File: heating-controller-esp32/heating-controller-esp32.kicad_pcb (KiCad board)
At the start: 2 copper layers, 96.6 x 146.8 mm, 110 parts, among them J1 431151015826, J10 76829-0104, J11 USB_C_Receptacle_USB2.0, J2 431151015826, J3 76829-0104, J4 76829-0104, J5 76829-0104, J6 76829-0104, J7 76829-0104, J8 76829-0104, J9 76829-0104, Q1 MBT3904DW1, U1 ESP32-WROOM-32U, U10 MOC3061M, U2 CP2102N-A01-GQFN28, U4 MOC3061M, U6 MOC3061M, U7 MOC3061M, U8 MOC3061M, U9 MOC3061M

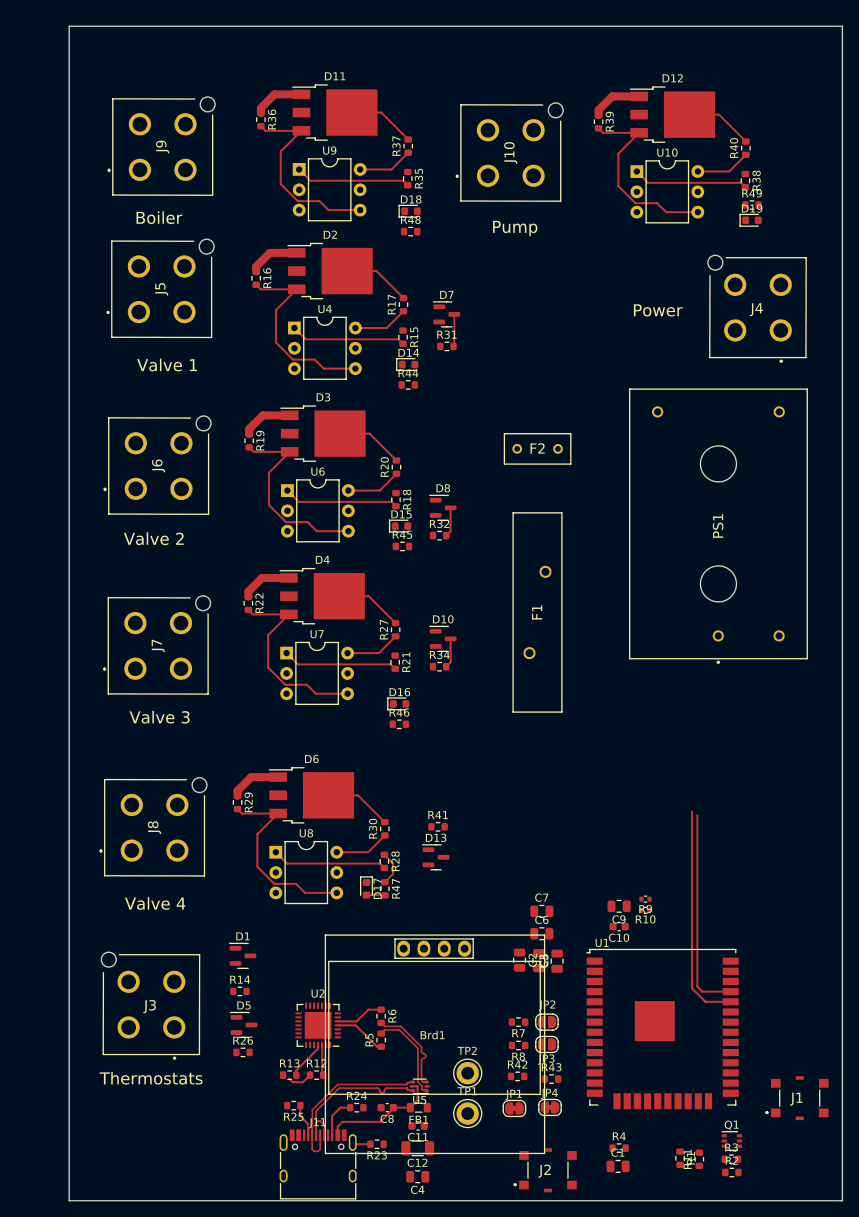
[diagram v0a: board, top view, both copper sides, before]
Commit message: Changed to Wago connectors; initial routing completed
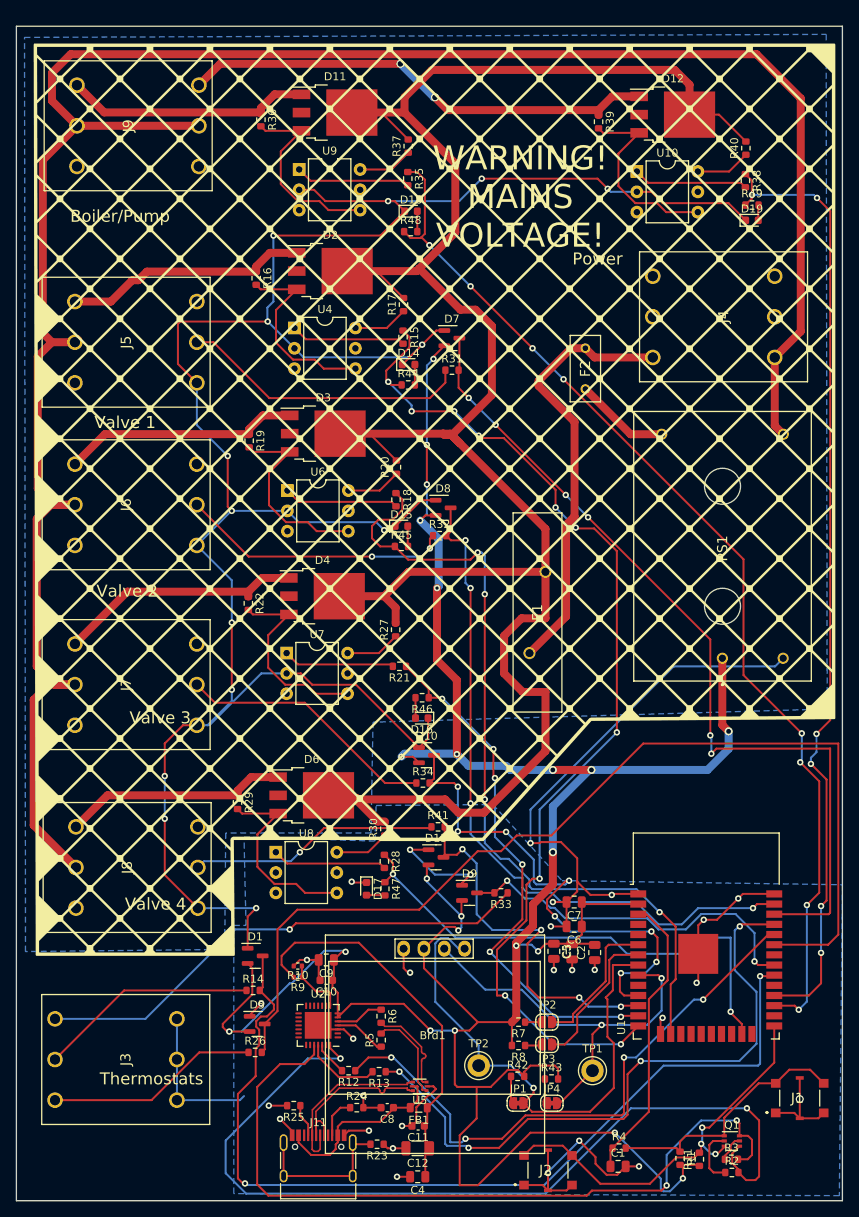
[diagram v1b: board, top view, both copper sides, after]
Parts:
- removed J10: 76829-0104, SamacSys_Parts:768290104
- added D9: ~, Package_TO_SOT_SMD:SOT-23, F.Cu at (66.5, 136.5)
- added R33: ~, Resistor_SMD:R_0603_1608Metric, F.Cu at (70.5, 136.5)
- J3, J4, J5, J6, J7, J8, J9: footprint SamacSys_Parts:768290104 -> SamacSys_Parts:736303
- U1: footprint RF_Module:ESP32-WROOM-32U -> RF_Module:ESP32-WROOM-32
- moved R9 44.5 mm to (45.1, 147.1)
- moved R10 44.0 mm to (45.1, 145.7)
- moved C9 37.2 mm to (48.6, 144.9)
- moved C10 37.2 mm to (48.6, 147.4)
- moved TP1 16.5 mm to (81.9, 158.8)
- moved R34 14.7 mm to (60.7, 122.8)
- moved D10 14.7 mm to (61.2, 119.3)
- moved J9 13.0 mm to (17.5, 35.6)
- moved J3 12.3 mm to (30.0, 162.4), turned to 90 degrees
- moved F2 11.7 mm to (81.0, 71.0), turned to -90 degrees
- moved R13 11.2 mm to (55.2, 158.9), turned to 180 degrees
- moved J5 10.8 mm to (17.2, 62.6)
- moved J6 10.3 mm to (17.2, 82.9)
- moved J7 10.3 mm to (17.2, 105.4)
- moved U1 10.0 mm to (96.1, 144.9)
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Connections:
- C10 pad 1: /ESP32/ESP_VDD -> +3V3
- C2 pad 2: /ESP32/ESP_VDD -> +3V3
- C3 pad 1: /ESP32/ESP_VDD -> +3V3
- C5 pad 2: /ESP32/ESP_VDD -> +3V3
- C6 pad 1: /ESP32/ESP_VDD -> +3V3
- C7 pad 1: /ESP32/ESP_VDD -> +3V3
- C9 pad 1: /ESP32/ESP_VDD -> +3V3
- D11 pad 1: /Boiler Out/Neutral -> /Boiler Out/Switched
- D12 pad 1: /Pump Out/Neutral -> /Pump Out/Switched
- D2 pad 1: /Valve Out 1/Neutral -> /Valve Out 1/Switched
- D3 pad 1: /Valve Out 2/Neutral -> /Valve Out 2/Switched
- D4 pad 1: /Valve Out 3/Neutral -> /Valve Out 3/Switched
- D6 pad 1: /Valve Out 4/Neutral -> /Valve Out 4/Switched
- J3 pad 1: /DHW_Thermostat -> GND
- J3 pad 2: GND -> /DHW_Thermostat
- J3 pad 3: /Spare_Thermostat -> GND
- J3 pad 4: GND -> /Spare_Thermostat
- J4 pad 1: unconnected-(J4-Pad1) -> NEUT
- J4 pad 2: Earth -> Net-(F1-Pad1)
- J4 pad 3: Net-(F1-Pad1) -> Earth
- J4 pad 4: NEUT -> unconnected-(J4-Pad4)
- J5 pad 1: /Valve_Microswitch_1 -> /Valve Out 1/Switched
- J5 pad 2: GND -> unconnected-(J5-Pad2)
- J5 pad 4: /Valve Out 1/Neutral -> /Valve_Microswitch_1
- J6 pad 1: /Valve_Microswitch_2 -> /Valve Out 2/Switched
- J6 pad 2: GND -> unconnected-(J6-Pad2)
- J6 pad 4: /Valve Out 2/Neutral -> /Valve_Microswitch_2
- J7 pad 1: /Valve_Microswitch_3 -> /Valve Out 3/Switched
- J7 pad 2: GND -> unconnected-(J7-Pad2)
- J7 pad 4: /Valve Out 3/Neutral -> /Valve_Microswitch_3
- J8 pad 1: /Valve_Microswitch_4 -> /Valve Out 4/Switched
- J8 pad 2: GND -> unconnected-(J8-Pad2)
- J8 pad 4: /Valve Out 4/Neutral -> /Valve_Microswitch_4
- J9 pad 1: Earth -> /Boiler Out/Switched
- J9 pad 2: unconnected-(J9-Pad2) -> /Pump Out/Switched
- J9 pad 4: /Boiler Out/Neutral -> NEUT
- R1 pad 1: /ESP32/ESP_VDD -> +3V3
- R11 pad 1: /ESP32/ESP_VDD -> +3V3
- R16 pad 1: /Valve Out 1/Neutral -> /Valve Out 1/Switched
- R19 pad 1: /Valve Out 2/Neutral -> /Valve Out 2/Switched
- R22 pad 1: /Valve Out 3/Neutral -> /Valve Out 3/Switched
- R29 pad 1: /Valve Out 4/Neutral -> /Valve Out 4/Switched
- R36 pad 1: /Boiler Out/Neutral -> /Boiler Out/Switched
- R39 pad 1: /Pump Out/Neutral -> /Pump Out/Switched
- R42 pad 2: 3.3V -> +3V3
- R43 pad 2: 3.3V -> +3V3
- U1 pad 2: /ESP32/ESP_VDD -> +3V3
- U2 pad 6: /ESP32/ESP_VDD -> +3V3
- U2 pad 7: /ESP32/ESP_VDD -> +3V3
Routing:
- net GND: track 0.00 -> 506.7 mm, vias 0 -> 43
- net +3V3: track 0.00 -> 347.5 mm, vias 0 -> 22
- net NEUT: track 0.00 -> 279.2 mm
- net LINE: track 50.6 -> 289.7 mm
- net /Boiler Out/Trigger: track 0.00 -> 134.1 mm, vias 0 -> 8
- net /ESP32/IO12: track 0.00 -> 132.4 mm, vias 0 -> 10
- net /ESP32/IO21: track 0.00 -> 128.3 mm
- net /ESP32/IO17: track 0.00 -> 120.3 mm, vias 0 -> 6
- net /ESP32/IO18: track 0.00 -> 116.1 mm, vias 0 -> 2
- net /ESP32/DTR: track 0.00 -> 111.8 mm, vias 0 -> 2
- net /ESP32/IO22: track 4.04 -> 107.8 mm, vias 0 -> 6
- net /ESP32/IO13: track 0.00 -> 102.6 mm, vias 0 -> 4
- net /ESP32/RTS: track 0.00 -> 96.5 mm, vias 0 -> 2
- net /ESP32/IO23: track 3.73 -> 87.8 mm, vias 0 -> 4
- net /ESP32/IO14: track 0.00 -> 66.3 mm, vias 0 -> 6
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- added copper zone on B.Cu, net Earth
- added copper zone on B.Cu, net GND
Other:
- board size 96.6 x 146.8 mm -> 103.3 x 146.8 mm
- board text added: "Boiler/Pump"
- board text added: "WARNING! MAINS VOLTAGE!"
- board text removed: "Boiler"
- board text removed: "Pump"

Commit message: Minor tweaks
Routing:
- net +3V3: track 347.5 -> 342.3 mm
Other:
- board text added: "Boot"
- board text added: "Reset"
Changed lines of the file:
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@@
+    (effects (font (size 1.5 1.5) (thickness 0.3)))
+  )
+  (gr_text "Reset" (at 107.95 167.386) (layer "F.SilkS")
     (effects (font (size 1.5 1.5) (thickness 0.3)))
   )
@@
     (effects (font (size 1.5 1.5) (thickness 0.3)))
   )
-  (gr_text "Power" (at 82.55 57.277) (layer "F.SilkS")
+  (gr_text "Power" (at 82.677 62.484) (layer "F.SilkS")
     (effects (font (size 1.5 1.5) (thickness 0.3)))
   )
   (gr_text "Boiler/Pump" (at 22.86 51.943) (layer "F.SilkS")
+    (effects (font (size 1.5 1.5) (thickness 0.3)))
+  )
+  (gr_text "Boot" (at 67.056 170.942) (layer "F.SilkS")
     (effects (font (size 1.5 1.5) (thickness 0.3)))
   )
@@
   (segment (start 72.39 142.748) (end 72.39 143.129) (width 1) (layer "F.Cu") (net 5))
   (segment (start 64.9605 109.9185) (end 62.484 107.442) (width 1) (layer "F.Cu") (net 5))
-  (segment (start 67.437 164.719) (end 65.315489 166.840511) (width 0.25) (layer "F.Cu") (net 5))
   (segment (start 76.068 142.88) (end 75.1205 143.8275) (width 0.25) (layer "F.Cu") (net 5))
   (segment (start 77.089 142.88) (end 82.042 142.88) (width 0.25) (layer "F.Cu") (net 5))
   (segment (start 71.84552 155.60152) (end 71.84552 152.68052) (width 0.25) (layer "F.Cu") (net 5))
   (segment (start 61.026 89.342) (end 60.3885 89.9795) (width 0.25) (layer "F.Cu") (net 5))
+  (segment (start 65.315489 166.840511) (end 67.437 164.719) (width 0.25) (layer "F.Cu") (net 5))
+  (segment (start 65.315489 169.380511) (end 65.315489 166.840511) (width 0.25) (layer "F.Cu") (net 5))
   (segment (start 98.151 115.55) (end 98.933 116.332) (width 1) (layer "F.Cu") (net 5))
   (segment (start 73.38352 159.46252) (end 73.38352 158.89948) (width 0.25) (layer "F.Cu") (net 5))
@@
   (segment (start 77.089 142.88) (end 76.068 142.88) (width 0.25) (layer "F.Cu") (net 5))
   (segment (start 60.85 145.94) (end 60.85 143.498) (width 0.25) (layer "F.Cu") (net 5))
-  (segment (start 74.168 166.497) (end 84.709 166.497) (width 0.25) (layer "F.Cu") (net 5))
   (segment (start 50.607 143.891) (end 49.591 144.907) (width 0.25) (layer "F.Cu") (net 5))
   (segment (start 35.697783 152.908) (end 35.697783 153.299783) (width 0.25) (layer "F.Cu") (net 5))
@@
   (segment (start 38.8135 145.349) (end 39.39652 145.93202) (width 0.25) (layer "F.Cu") (net 5))
   (segment (start 51.054 143.891) (end 50.607 143.891) (width 0.25) (layer "F.Cu") (net 5))
-  (segment (start 67.437 160.782) (end 67.437 164.719) (width 0.25) (layer "F.Cu") (net 5))
   (segment (start 80.579 137.668) (end 80.833 137.922) (width 0.25) (layer "F.Cu") (net 5))
   (segment (start 92.86352 170.52352) (end 95.14952 170.52352) (width 0.25) (layer "F.Cu") (net 5))
@@
   (segment (start 67.59052 152.68052) (end 60.85 145.94) (width 0.25) (layer "F.Cu") (net 5))
   (segment (start 74.168 158.115) (end 77.216 158.115) (width 0.25) (layer "F.Cu") (net 5))
+  (segment (start 73.025 166.497) (end 70.141489 169.380511) (width 0.25) (layer "F.Cu") (net 5))
   (segment (start 72.584 158.663) (end 73.38352 159.46252) (width 0.25) (layer "F.Cu") (net 5))
+  (segment (start 84.709 166.497) (end 73.025 166.497) (width 0.25) (layer "F.Cu") (net 5))
   (segment (start 49.416 148.349) (end 50.075 149.008) (width 0.25) (layer "F.Cu") (net 5))
-  (segment (start 65.315489 173.069969) (end 67.595031 173.069969) (width 0.25) (layer "F.Cu") (net 5))
   (segment (start 76.962 131.445) (end 76.962 135.477338) (width 1) (layer "F.Cu") (net 5))
   (segment (start 98.151 107.197) (end 98.151 115.55) (width 1) (layer "F.Cu") (net 5))
@@
   (segment (start 62.3085 89.342) (end 61.026 89.342) (width 0.25) (layer "F.Cu") (net 5))
   (segment (start 49.416 147.447) (end 49.416 148.349) (width 0.25) (layer "F.Cu") (net 5))
-  (segment (start 67.595031 173.069969) (end 74.168 166.497) (width 0.25) (layer "F.Cu") (net 5))
   (segment (start 39.39652 149.209263) (end 35.697783 152.908) (width 0.25) (layer "F.Cu") (net 5))
   (segment (start 67.437 160.782) (end 69.197257 160.782) (width 0.25) (layer "F.Cu") (net 5))
@@
   (segment (start 64.7065 160.4645) (end 65.024 160.782) (width 0.25) (layer "F.Cu") (net 5))
   (segment (start 50.075 152.087) (end 51.76752 150.39448) (width 0.25) (layer "F.Cu") (net 5))
-  (segment (start 65.315489 166.840511) (end 65.315489 173.069969) (width 0.25) (layer "F.Cu") (net 5))
   (segment (start 64.7065 153.7335) (end 64.7065 160.4645) (width 0.25) (layer "F.Cu") (net 5))
   (segment (start 49.591 147.272) (end 49.416 147.447) (width 0.25) (layer "F.Cu") (net 5))
   (segment (start 93.218 170.878) (end 92.86352 170.52352) (width 0.25) (layer "F.Cu") (net 5))
+  (segment (start 70.141489 169.380511) (end 65.315489 169.380511) (width 0.25) (layer "F.Cu") (net 5))
   (segment (start 76.962 135.477338) (end 74.48452 137.954818) (width 1) (layer "F.Cu") (net 5))
   (segment (start 61.214 80.518) (end 61.214 85.471) (width 0.25) (layer "F.Cu") (net 5))
+  (segment (start 67.437 164.719) (end 67.437 160.782) (width 0.25) (layer "F.Cu") (net 5))
   (segment (start 93.218 172.212) (end 93.218 170.878) (width 0.25) (layer "F.Cu") (net 5))
   (segment (start 51.76752 150.39448) (end 58.31948 150.39448) (width 0.25) (layer "F.Cu") (net 5))
@@
         (xy 37.211 144.399)
         (xy 12.319 144.399)
-        (xy 12.065 30.353)
-        (xy 112.268 30.353)
+        (xy 12.319 29.083)
+        (xy 112.268 28.956)
       )
     )

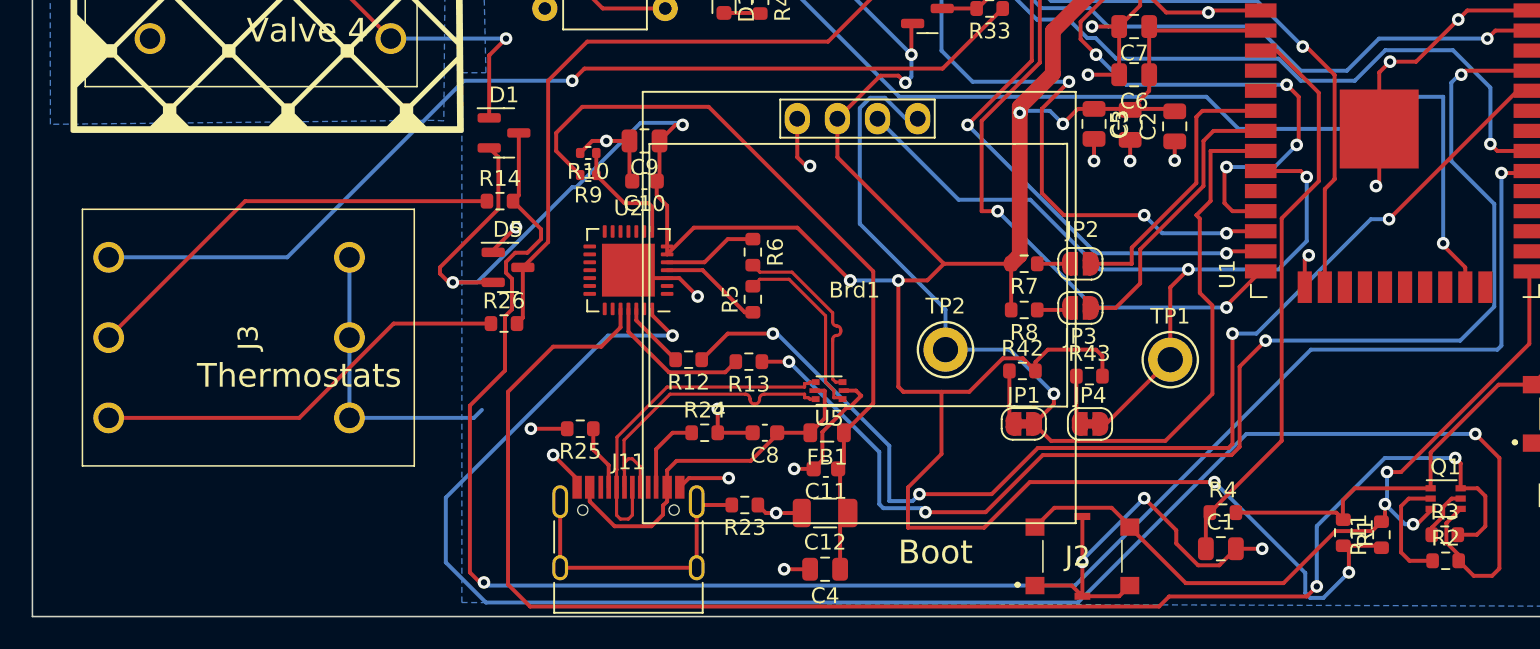
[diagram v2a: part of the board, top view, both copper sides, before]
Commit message: Added additional spare thermostat inputs
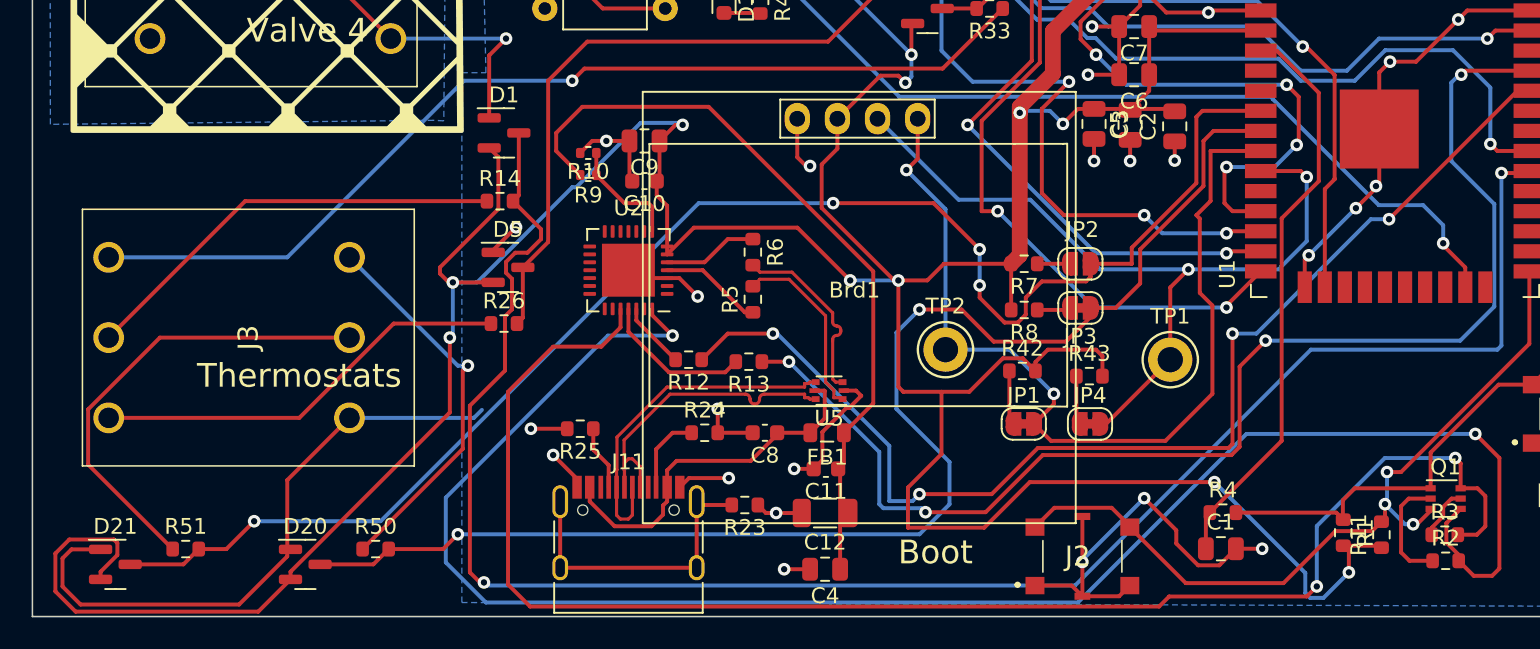
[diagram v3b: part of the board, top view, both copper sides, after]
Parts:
- added D20: ~, Package_TO_SOT_SMD:SOT-23, F.Cu at (27.2, 171.7)
- added D21: ~, Package_TO_SOT_SMD:SOT-23, F.Cu at (15.2, 171.7)
- added R50: ~, Resistor_SMD:R_0603_1608Metric, F.Cu at (31.6, 170.7)
- added R51: ~, Resistor_SMD:R_0603_1608Metric, F.Cu at (19.6, 170.7)
- JP2: value SolderJumper_2_Open -> SolderJumper_2_Bridged
- JP3: value SolderJumper_2_Open -> SolderJumper_2_Bridged; footprint Jumper:SolderJumper-2_P1.3mm_Open_RoundedPad1.0x1.5mm -> Jumper:SolderJumper-2_P1.3mm_Bridged_RoundedPad1.0x1.5mm
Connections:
- J3 pad 3: GND -> /Spare_Thermostat_3
- J3 pad 5: GND -> /Spare_Thermostat_4
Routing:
- net /ESP32/IO34: track 17.8 -> 95.6 mm, vias 0 -> 4
- net /ESP32/IO35: track 18.3 -> 87.0 mm, vias 0 -> 2
- net +3V3: track 342.3 -> 391.9 mm, vias 22 -> 23
- net /Spare_Thermostat_3: track 0.00 -> 29.5 mm
- net GND: track 506.7 -> 533.4 mm, vias 43 -> 44
- net /Spare_Thermostat_4: track 0.00 -> 24.7 mm, vias 0 -> 1
- net /ESP32/IO15: track 64.2 -> 57.8 mm
- net /ESP32/IO32: track 64.8 -> 58.7 mm, vias 1 -> 2

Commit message: Mounting holes, a few more tweaks
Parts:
- added H1: MountingHole, MountingHole:MountingHole_3.2mm_M3_DIN965, F.Cu at (13.5, 31.8)
- added H2: MountingHole, MountingHole:MountingHole_3.2mm_M3_DIN965, F.Cu at (13.5, 171.4)
- added H3: MountingHole, MountingHole:MountingHole_3.2mm_M3_DIN965, F.Cu at (109.6, 171.4)
- added H4: MountingHole, MountingHole:MountingHole_3.2mm_M3_DIN965, F.Cu at (109.6, 31.8)
- added H5: MountingHole, MountingHole:MountingHole_3.2mm_M3_DIN965, F.Cu at (39.6, 50.2)
- added H6: MountingHole, MountingHole:MountingHole_3.2mm_M3_DIN965, F.Cu at (83.8, 116.0)
- added H7: MountingHole, MountingHole:MountingHole_3.2mm_M3_DIN965, F.Cu at (39.6, 117.2)
- added H8: MountingHole, MountingHole:MountingHole_3.2mm_M3_DIN965, F.Cu at (74.3, 60.6)
- moved J9 5.72 mm to (17.2, 41.3)
- moved D21 4.35 mm to (19.5, 171.7)
- moved R51 4.35 mm to (24.0, 170.7)
- moved D20 2.58 mm to (29.8, 171.7)
- moved R50 2.58 mm to (34.2, 170.7)
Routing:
- net NEUT: track 279.2 -> 257.3 mm, vias 0 -> 2
- net +3V3: track 391.9 -> 386.0 mm
- net /Pump Out/Switched: track 59.9 -> 65.7 mm
- net /Spare_Thermostat_3: track 29.5 -> 34.2 mm
- net /ESP32/IO34: track 95.6 -> 91.3 mm
- net /ESP32/IO12: track 132.4 -> 136.2 mm
- net /Boiler Out/Switched: track 30.9 -> 33.8 mm
- net /ESP32/IO35: track 87.0 -> 84.4 mm
- net GND: track 533.4 -> 531.0 mm
- net /Spare_Thermostat_4: track 24.7 -> 23.8 mm
